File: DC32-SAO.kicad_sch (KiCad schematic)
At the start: 11 parts, among them J1 Conn_01x06_Male

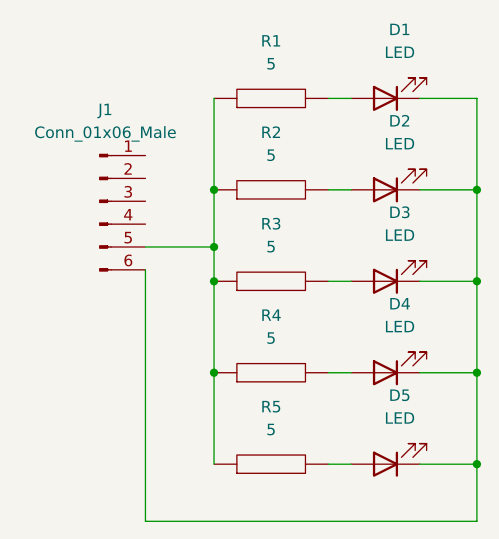
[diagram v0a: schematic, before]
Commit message: Changed orientation of power pins.
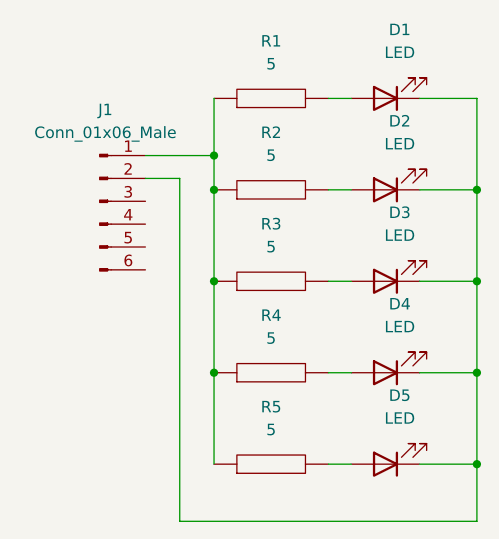
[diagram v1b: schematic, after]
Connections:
- net at D1.1 (K), D2.1 (K), D3.1 (K)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: now also J1.2 (Pin_2); no longer J1.6 (Pin_6)
- net at R1.1, R2.1, R3.1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: now also J1.1 (Pin_1); no longer J1.5 (Pin_5)
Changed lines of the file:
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@@
 (kicad_sch (version 20211123) (generator eeschema)
   (paper "A4")
+  (junction (at 85.09 53.34) (diameter 0) (color 0 0 0 0)
+  )
   (junction (at 85.09 57.15) (diameter 0) (color 0 0 0 0)
   )
@@
   )
   (junction (at 114.3 87.63) (diameter 0) (color 0 0 0 0)
-  )
-  (junction (at 85.09 63.5) (diameter 0) (color 0 0 0 0)
   )
   (junction (at 114.3 67.31) (diameter 0) (color 0 0 0 0)
@@
     (stroke (width 0) (type default) (color 0 0 0 0))
   )
+  (wire (pts (xy 77.47 53.34) (xy 85.09 53.34))
+    (stroke (width 0) (type default) (color 0 0 0 0))
+  )
   (wire (pts (xy 107.95 46.99) (xy 114.3 46.99))
     (stroke (width 0) (type default) (color 0 0 0 0))
@@
     (stroke (width 0) (type default) (color 0 0 0 0))
   )
-  (wire (pts (xy 77.47 63.5) (xy 85.09 63.5))
+  (wire (pts (xy 77.47 55.88) (xy 81.28 55.88))
     (stroke (width 0) (type default) (color 0 0 0 0))
   )
@@
     (stroke (width 0) (type default) (color 0 0 0 0))
   )
-  (wire (pts (xy 114.3 93.98) (xy 77.47 93.98))
+  (wire (pts (xy 114.3 93.98) (xy 81.28 93.98))
     (stroke (width 0) (type default) (color 0 0 0 0))
   )
@@
     (stroke (width 0) (type default) (color 0 0 0 0))
   )
+  (wire (pts (xy 85.09 53.34) (xy 85.09 57.15))
+    (stroke (width 0) (type default) (color 0 0 0 0))
+  )
   (wire (pts (xy 107.95 77.47) (xy 114.3 77.47))
     (stroke (width 0) (type default) (color 0 0 0 0))
@@
     (stroke (width 0) (type default) (color 0 0 0 0))
   )
-  (wire (pts (xy 85.09 46.99) (xy 85.09 57.15))
+  (wire (pts (xy 85.09 46.99) (xy 85.09 53.34))
     (stroke (width 0) (type default) (color 0 0 0 0))
   )
-  (wire (pts (xy 85.09 63.5) (xy 85.09 67.31))
+  (wire (pts (xy 85.09 57.15) (xy 85.09 67.31))
     (stroke (width 0) (type default) (color 0 0 0 0))
   )
   (wire (pts (xy 97.79 57.15) (xy 100.33 57.15))
-    (stroke (width 0) (type default) (color 0 0 0 0))
-  )
-  (wire (pts (xy 77.47 93.98) (xy 77.47 66.04))
     (stroke (width 0) (type default) (color 0 0 0 0))
   )
@@
     (stroke (width 0) (type default) (color 0 0 0 0))
   )
+  (wire (pts (xy 81.28 55.88) (xy 81.28 93.98))
+    (stroke (width 0) (type default) (color 0 0 0 0))
+  )
   (wire (pts (xy 85.09 77.47) (xy 85.09 87.63))
     (stroke (width 0) (type default) (color 0 0 0 0))
@@
     (stroke (width 0) (type default) (color 0 0 0 0))
   )
-  (wire (pts (xy 85.09 63.5) (xy 85.09 57.15))
-    (stroke (width 0) (type default) (color 0 0 0 0))
-  )

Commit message: Minting v0.2
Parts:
- D1, D2, D3, D4, D5: footprint LEDs:LED_0606_HandSoldering -> LEDs:LED_0606
- R1, R2, R3, R4, R5: footprint Resistor_SMD:R_0603_1608Metric_Pad0.98x0.95mm_HandSolder -> Resistor_SMD:R_0603_1608Metric
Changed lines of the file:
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@@
     (property "Reference" "D3" (id 0) (at 105.7275 59.69 0))
     (property "Value" "LED" (id 1) (at 105.7275 62.23 0))
-    (property "Footprint" "LEDs:LED_0606_HandSoldering" (id 2) (at 104.14 67.31 0)
+    (property "Footprint" "LEDs:LED_0606" (id 2) (at 104.14 67.31 0)
       (effects (font (size 1.27 1.27)) hide)
     )
@@
     (property "Reference" "R5" (id 0) (at 91.44 81.28 90))
     (property "Value" "5" (id 1) (at 91.44 83.82 90))
-    (property "Footprint" "Resistor_SMD:R_0603_1608Metric_Pad0.98x0.95mm_HandSolder" (id 2) (at 91.44 87.63 0)
+    (property "Footprint" "Resistor_SMD:R_0603_1608Metric" (id 2) (at 91.44 87.63 0)
       (effects (font (size 1.27 1.27)) hide)
     )
@@
     (property "Reference" "D1" (id 0) (at 105.7275 39.37 0))
     (property "Value" "LED" (id 1) (at 105.7275 41.91 0))
-    (property "Footprint" "LEDs:LED_0606_HandSoldering" (id 2) (at 104.14 46.99 0)
+    (property "Footprint" "LEDs:LED_0606" (id 2) (at 104.14 46.99 0)
       (effects (font (size 1.27 1.27)) hide)
     )
@@
     (property "Reference" "R1" (id 0) (at 91.44 40.64 90))
     (property "Value" "5" (id 1) (at 91.44 43.18 90))
-    (property "Footprint" "Resistor_SMD:R_0603_1608Metric_Pad0.98x0.95mm_HandSolder" (id 2) (at 91.44 46.99 0)
+    (property "Footprint" "Resistor_SMD:R_0603_1608Metric" (id 2) (at 91.44 46.99 0)
       (effects (font (size 1.27 1.27)) hide)
     )
@@
     (property "Reference" "R3" (id 0) (at 91.44 60.96 90))
     (property "Value" "5" (id 1) (at 91.44 63.5 90))
-    (property "Footprint" "Resistor_SMD:R_0603_1608Metric_Pad0.98x0.95mm_HandSolder" (id 2) (at 91.44 67.31 0)
+    (property "Footprint" "Resistor_SMD:R_0603_1608Metric" (id 2) (at 91.44 67.31 0)
       (effects (font (size 1.27 1.27)) hide)
     )
@@
     (property "Reference" "D5" (id 0) (at 105.7275 80.01 0))
     (property "Value" "LED" (id 1) (at 105.7275 82.55 0))
-    (property "Footprint" "LEDs:LED_0606_HandSoldering" (id 2) (at 104.14 87.63 0)
+    (property "Footprint" "LEDs:LED_0606" (id 2) (at 104.14 87.63 0)
       (effects (font (size 1.27 1.27)) hide)
     )
@@
     (property "Reference" "R4" (id 0) (at 91.44 71.12 90))
     (property "Value" "5" (id 1) (at 91.44 73.66 90))
-    (property "Footprint" "Resistor_SMD:R_0603_1608Metric_Pad0.98x0.95mm_HandSolder" (id 2) (at 91.44 77.47 0)
+    (property "Footprint" "Resistor_SMD:R_0603_1608Metric" (id 2) (at 91.44 77.47 0)
       (effects (font (size 1.27 1.27)) hide)
     )
@@
     (property "Reference" "R2" (id 0) (at 91.44 50.8 90))
     (property "Value" "5" (id 1) (at 91.44 53.34 90))
-    (property "Footprint" "Resistor_SMD:R_0603_1608Metric_Pad0.98x0.95mm_HandSolder" (id 2) (at 91.44 57.15 0)
+    (property "Footprint" "Resistor_SMD:R_0603_1608Metric" (id 2) (at 91.44 57.15 0)
       (effects (font (size 1.27 1.27)) hide)
     )
@@
     (property "Reference" "D4" (id 0) (at 105.7275 69.85 0))
     (property "Value" "LED" (id 1) (at 105.7275 72.39 0))
-    (property "Footprint" "LEDs:LED_0606_HandSoldering" (id 2) (at 104.14 77.47 0)
+    (property "Footprint" "LEDs:LED_0606" (id 2) (at 104.14 77.47 0)
       (effects (font (size 1.27 1.27)) hide)
     )
@@
     (property "Reference" "D2" (id 0) (at 105.7275 49.53 0))
     (property "Value" "LED" (id 1) (at 105.7275 52.07 0))
-    (property "Footprint" "LEDs:LED_0606_HandSoldering" (id 2) (at 104.14 57.15 0)
+    (property "Footprint" "LEDs:LED_0606" (id 2) (at 104.14 57.15 0)
       (effects (font (size 1.27 1.27)) hide)
     )
@@
   (symbol_instances
     (path "/303269a8-04f0-413a-84f6-c72d1bf91057"
-      (reference "D1") (unit 1) (value "LED") (footprint "LEDs:LED_0606_HandSoldering")
+      (reference "D1") (unit 1) (value "LED") (footprint "LEDs:LED_0606")
     )
     (path "/fc3462c2-5190-4505-9e25-4540f82e78cb"
-      (reference "D2") (unit 1) (value "LED") (footprint "LEDs:LED_0606_HandSoldering")
+      (reference "D2") (unit 1) (value "LED") (footprint "LEDs:LED_0606")
     )
     (path "/0b820862-83d5-4dc0-a8cf-9bd5f1a499cc"
-      (reference "D3") (unit 1) (value "LED") (footprint "LEDs:LED_0606_HandSoldering")
+      (reference "D3") (unit 1) (value "LED") (footprint "LEDs:LED_0606")
     )
     (path "/f085cf9f-e2ae-49e0-961e-63b6cbb4d40f"
-      (reference "D4") (unit 1) (value "LED") (footprint "LEDs:LED_0606_HandSoldering")
+      (reference "D4") (unit 1) (value "LED") (footprint "LEDs:LED_0606")
     )
     (path "/b1e9978e-60c7-4b92-827b-0033dd1b8c0c"
-      (reference "D5") (unit 1) (value "LED") (footprint "LEDs:LED_0606_HandSoldering")
+      (reference "D5") (unit 1) (value "LED") (footprint "LEDs:LED_0606")
     )
     (path "/5681b4fd-442e-49d7-8fe1-5d17e8cfa0a0"
@@
     )
     (path "/3224a758-6c5e-466b-a995-832667ce7042"
-      (reference "R1") (unit 1) (value "5") (footprint "Resistor_SMD:R_0603_1608Metric_Pad0.98x0.95mm_HandSolder")
+      (reference "R1") (unit 1) (value "5") (footprint "Resistor_SMD:R_0603_1608Metric")
     )
     (path "/e52018b4-0166-44c3-88cb-627e4c30fa0d"
-      (reference "R2") (unit 1) (value "5") (footprint "Resistor_SMD:R_0603_1608Metric_Pad0.98x0.95mm_HandSolder")
+      (reference "R2") (unit 1) (value "5") (footprint "Resistor_SMD:R_0603_1608Metric")
     )
     (path "/8fae0e04-1839-4e2c-8d18-18ef127a06b2"
-      (reference "R3") (unit 1) (value "5") (footprint "Resistor_SMD:R_0603_1608Metric_Pad0.98x0.95mm_HandSolder")
+      (reference "R3") (unit 1) (value "5") (footprint "Resistor_SMD:R_0603_1608Metric")
     )
     (path "/d6cef32c-fe73-4c94-b806-d19f76d5f19f"
-      (reference "R4") (unit 1) (value "5") (footprint "Resistor_SMD:R_0603_1608Metric_Pad0.98x0.95mm_HandSolder")
+      (reference "R4") (unit 1) (value "5") (footprint "Resistor_SMD:R_0603_1608Metric")
     )
     (path "/0c8e1220-c447-4528-8dc0-9ae09eaa4b36"
-      (reference "R5") (unit 1) (value "5") (footprint "Resistor_SMD:R_0603_1608Metric_Pad0.98x0.95mm_HandSolder")
+      (reference "R5") (unit 1) (value "5") (footprint "Resistor_SMD:R_0603_1608Metric")
     )
   )

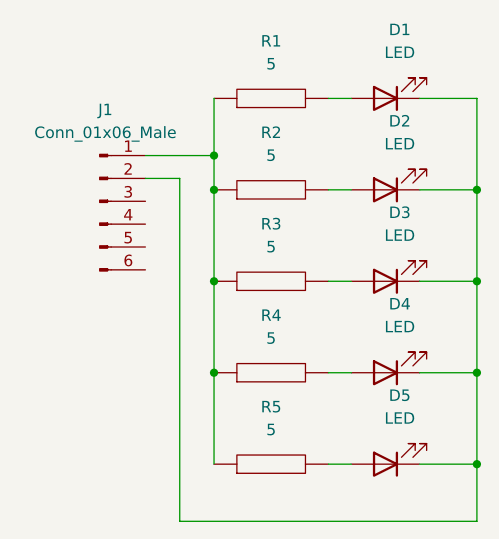
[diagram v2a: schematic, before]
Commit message: Added resistor values used by manufacturer.
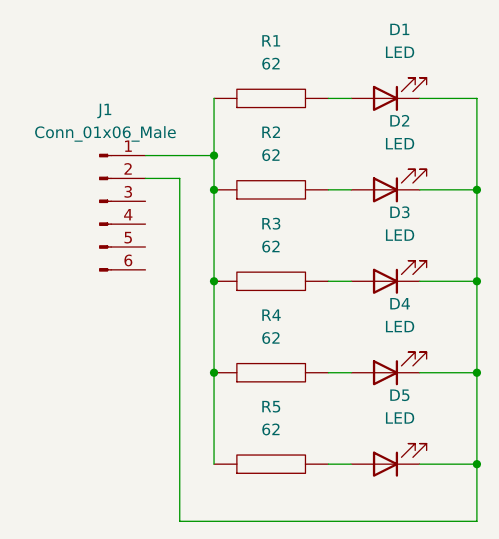
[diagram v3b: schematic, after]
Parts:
- R1, R2, R3, R4, R5: value 5 -> 62
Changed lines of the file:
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@@
     (in_bom yes) (on_board yes) (fields_autoplaced)
     (property "Reference" "R5" (id 0) (at 91.44 81.28 90))
-    (property "Value" "5" (id 1) (at 91.44 83.82 90))
+    (property "Value" "62" (id 1) (at 91.44 83.82 90))
     (property "Footprint" "Resistor_SMD:R_0603_1608Metric" (id 2) (at 91.44 87.63 0)
       (effects (font (size 1.27 1.27)) hide)
@@
     (in_bom yes) (on_board yes) (fields_autoplaced)
     (property "Reference" "R1" (id 0) (at 91.44 40.64 90))
-    (property "Value" "5" (id 1) (at 91.44 43.18 90))
+    (property "Value" "62" (id 1) (at 91.44 43.18 90))
     (property "Footprint" "Resistor_SMD:R_0603_1608Metric" (id 2) (at 91.44 46.99 0)
       (effects (font (size 1.27 1.27)) hide)
@@
     (in_bom yes) (on_board yes) (fields_autoplaced)
     (property "Reference" "R3" (id 0) (at 91.44 60.96 90))
-    (property "Value" "5" (id 1) (at 91.44 63.5 90))
+    (property "Value" "62" (id 1) (at 91.44 63.5 90))
     (property "Footprint" "Resistor_SMD:R_0603_1608Metric" (id 2) (at 91.44 67.31 0)
       (effects (font (size 1.27 1.27)) hide)
@@
     (in_bom yes) (on_board yes) (fields_autoplaced)
     (property "Reference" "R4" (id 0) (at 91.44 71.12 90))
-    (property "Value" "5" (id 1) (at 91.44 73.66 90))
+    (property "Value" "62" (id 1) (at 91.44 73.66 90))
     (property "Footprint" "Resistor_SMD:R_0603_1608Metric" (id 2) (at 91.44 77.47 0)
       (effects (font (size 1.27 1.27)) hide)
@@
     (in_bom yes) (on_board yes) (fields_autoplaced)
     (property "Reference" "R2" (id 0) (at 91.44 50.8 90))
-    (property "Value" "5" (id 1) (at 91.44 53.34 90))
+    (property "Value" "62" (id 1) (at 91.44 53.34 90))
     (property "Footprint" "Resistor_SMD:R_0603_1608Metric" (id 2) (at 91.44 57.15 0)
       (effects (font (size 1.27 1.27)) hide)
@@
     )
     (path "/3224a758-6c5e-466b-a995-832667ce7042"
-      (reference "R1") (unit 1) (value "5") (footprint "Resistor_SMD:R_0603_1608Metric")
+      (reference "R1") (unit 1) (value "62") (footprint "Resistor_SMD:R_0603_1608Metric")
     )
     (path "/e52018b4-0166-44c3-88cb-627e4c30fa0d"
-      (reference "R2") (unit 1) (value "5") (footprint "Resistor_SMD:R_0603_1608Metric")
+      (reference "R2") (unit 1) (value "62") (footprint "Resistor_SMD:R_0603_1608Metric")
     )
     (path "/8fae0e04-1839-4e2c-8d18-18ef127a06b2"
-      (reference "R3") (unit 1) (value "5") (footprint "Resistor_SMD:R_0603_1608Metric")
+      (reference "R3") (unit 1) (value "62") (footprint "Resistor_SMD:R_0603_1608Metric")
     )
     (path "/d6cef32c-fe73-4c94-b806-d19f76d5f19f"
-      (reference "R4") (unit 1) (value "5") (footprint "Resistor_SMD:R_0603_1608Metric")
+      (reference "R4") (unit 1) (value "62") (footprint "Resistor_SMD:R_0603_1608Metric")
     )
     (path "/0c8e1220-c447-4528-8dc0-9ae09eaa4b36"
-      (reference "R5") (unit 1) (value "5") (footprint "Resistor_SMD:R_0603_1608Metric")
+      (reference "R5") (unit 1) (value "62") (footprint "Resistor_SMD:R_0603_1608Metric")
     )
   )

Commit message: Set LEDs to 3mm round top.
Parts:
- D1, D2, D3, D4, D5: footprint LEDs:LED_0606 -> LED_THT:LED_D3.0mm
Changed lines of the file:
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@@
     (property "Reference" "D3" (id 0) (at 105.7275 59.69 0))
     (property "Value" "LED" (id 1) (at 105.7275 62.23 0))
-    (property "Footprint" "LEDs:LED_0606" (id 2) (at 104.14 67.31 0)
+    (property "Footprint" "LED_THT:LED_D3.0mm" (id 2) (at 104.14 67.31 0)
       (effects (font (size 1.27 1.27)) hide)
     )
@@
     (property "Reference" "D1" (id 0) (at 105.7275 39.37 0))
     (property "Value" "LED" (id 1) (at 105.7275 41.91 0))
-    (property "Footprint" "LEDs:LED_0606" (id 2) (at 104.14 46.99 0)
+    (property "Footprint" "LED_THT:LED_D3.0mm" (id 2) (at 104.14 46.99 0)
       (effects (font (size 1.27 1.27)) hide)
     )
@@
     (property "Reference" "D5" (id 0) (at 105.7275 80.01 0))
     (property "Value" "LED" (id 1) (at 105.7275 82.55 0))
-    (property "Footprint" "LEDs:LED_0606" (id 2) (at 104.14 87.63 0)
+    (property "Footprint" "LED_THT:LED_D3.0mm" (id 2) (at 104.14 87.63 0)
       (effects (font (size 1.27 1.27)) hide)
     )
@@
     (property "Reference" "D4" (id 0) (at 105.7275 69.85 0))
     (property "Value" "LED" (id 1) (at 105.7275 72.39 0))
-    (property "Footprint" "LEDs:LED_0606" (id 2) (at 104.14 77.47 0)
+    (property "Footprint" "LED_THT:LED_D3.0mm" (id 2) (at 104.14 77.47 0)
       (effects (font (size 1.27 1.27)) hide)
     )
@@
     (property "Reference" "D2" (id 0) (at 105.7275 49.53 0))
     (property "Value" "LED" (id 1) (at 105.7275 52.07 0))
-    (property "Footprint" "LEDs:LED_0606" (id 2) (at 104.14 57.15 0)
+    (property "Footprint" "LED_THT:LED_D3.0mm" (id 2) (at 104.14 57.15 0)
       (effects (font (size 1.27 1.27)) hide)
     )
@@
   (symbol_instances
     (path "/303269a8-04f0-413a-84f6-c72d1bf91057"
-      (reference "D1") (unit 1) (value "LED") (footprint "LEDs:LED_0606")
+      (reference "D1") (unit 1) (value "LED") (footprint "LED_THT:LED_D3.0mm")
     )
     (path "/fc3462c2-5190-4505-9e25-4540f82e78cb"
-      (reference "D2") (unit 1) (value "LED") (footprint "LEDs:LED_0606")
+      (reference "D2") (unit 1) (value "LED") (footprint "LED_THT:LED_D3.0mm")
     )
     (path "/0b820862-83d5-4dc0-a8cf-9bd5f1a499cc"
-      (reference "D3") (unit 1) (value "LED") (footprint "LEDs:LED_0606")
+      (reference "D3") (unit 1) (value "LED") (footprint "LED_THT:LED_D3.0mm")
     )
     (path "/f085cf9f-e2ae-49e0-961e-63b6cbb4d40f"
-      (reference "D4") (unit 1) (value "LED") (footprint "LEDs:LED_0606")
+      (reference "D4") (unit 1) (value "LED") (footprint "LED_THT:LED_D3.0mm")
     )
     (path "/b1e9978e-60c7-4b92-827b-0033dd1b8c0c"
-      (reference "D5") (unit 1) (value "LED") (footprint "LEDs:LED_0606")
+      (reference "D5") (unit 1) (value "LED") (footprint "LED_THT:LED_D3.0mm")
     )
     (path "/5681b4fd-442e-49d7-8fe1-5d17e8cfa0a0"
